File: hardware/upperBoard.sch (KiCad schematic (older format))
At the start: 16 parts, among them J1 Program interface, J2 Conn_02x09_Odd_Even, Q1 S8050, Q2 S8050, SW1 Reset, SW2 Prog, U1 ESP-12F, U2 PCF8575

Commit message: started to replace PCF8575 with MCP23016 and separated LEDs with arrays
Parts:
- removed U2: PCF8575, Package_SO:SSOP-24_5.3x8.2mm_P0.65mm, symbol NXP:PCF8575
- added BAR?: HDSP-4830_2, Display:HDSP-4830, symbol LED:HDSP-4830_2
- added C?: C, symbol Device:C
- added IC?: MCP23016SO, microchip-dspic-SO-28W, symbol microchip-dspic:MCP23016SO
- added R?: R, symbol Device:R
- added RN?: R_Network08, Resistor_THT:R_Array_SIP9, symbol Device:R_Network08
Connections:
- wire segments 148 -> 101

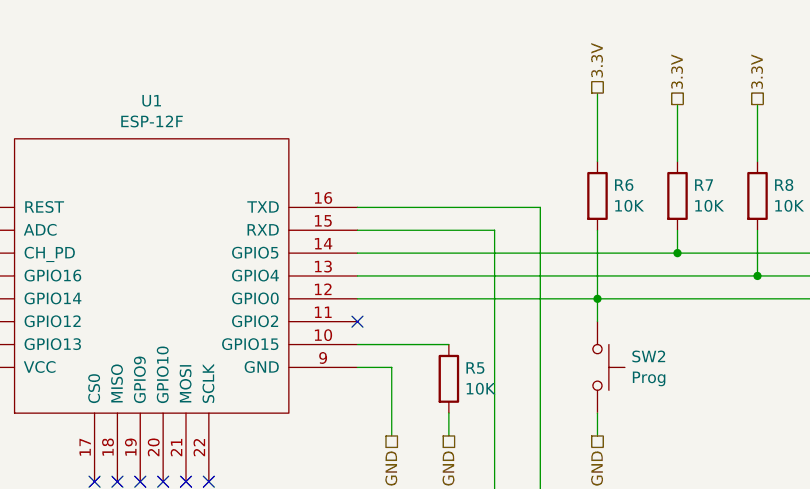
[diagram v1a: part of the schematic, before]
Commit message: renamed hardware files
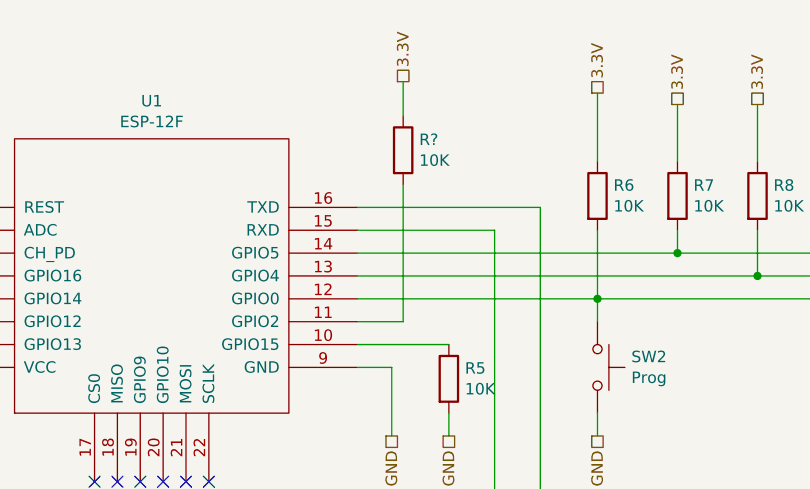
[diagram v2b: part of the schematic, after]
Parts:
- added R?: 10K, Resistor_SMD:R_0201_0603Metric, symbol Device:R
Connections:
- wire segments 101 -> 104
- no-connect marks 13 -> 12
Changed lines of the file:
@@
 NoConn ~ 2600 3000
 NoConn ~ 2500 3000
-NoConn ~ 3650 2300
 NoConn ~ 1850 1900
 NoConn ~ 1850 2100
@@
 	-1   0    0    1
 $EndComp
+$Comp
+L Device:R R?
+U 1 1 5D9733D1
+P 3850 1550
+F 0 "R?" H 3920 1596 50  0000 L CNN
+F 1 "10K" H 3920 1505 50  0000 L CNN
+F 2 "Resistor_SMD:R_0201_0603Metric" V 3780 1550 50  0001 C CNN
+F 3 "~" H 3850 1550 50  0001 C CNN
+	1    3850 1550
+	1    0    0    -1
+$EndComp
+Text HLabel 3850 1250 1    50   UnSpc ~ 0
+3.3V
+Wire Wire Line
+	3850 1250 3850 1400
+Wire Wire Line
+	3850 1700 3850 2300
+Wire Wire Line
+	3850 2300 3650 2300
 $EndSCHEMATC

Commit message: replaced separated driver parts with driver chips and LED bars
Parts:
- removed J2: Conn_02x09_Odd_Even, symbol Connector_Generic:Conn_02x09_Odd_Even
- added BAR1: HDSP-4830_2, Display:HDSP-4830, symbol LED:HDSP-4830_2
- added J2: Conn_02x10_Odd_Even, symbol Connector_Generic:Conn_02x10_Odd_Even
- added RN1: R_Network08, Resistor_THT:R_Array_SIP9, symbol Device:R_Network08
- added U2, U4: A2982, Package_SO:SOIC-20W_7.5x12.8mm_P1.27mm, symbol Transistor_Array:A2982
- gave numbers to parts that had none: 6
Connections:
- net labels added: 1.0, 1.1, 1.2, 1.3, 1.4, 1.5, 1.6, 1.7, 12V
- net labels removed: upper3.3V, upperGND
- wire segments 104 -> 183
- no-connect marks 12 -> 20
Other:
- moved on the sheet: BAR2, C2, J1, Q1, Q2, R1, R10, R2, R3, R4, R5, R6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

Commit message: extracted relay to sub schematic to be able to multiply it
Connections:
- wire segments 183 -> 185
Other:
- moved on the sheet: J2
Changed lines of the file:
@@
 $Descr A4 11693 8268
 encoding utf-8
-Sheet 2 3
+Sheet 2 5
 Title ""
 Date ""
@@
 Wire Wire Line
 	3300 2600 4450 2600
-Text HLabel 5650 7550 0    50   UnSpc ~ 0
-3.3V
-Text HLabel 6550 7550 2    50   UnSpc ~ 0
+Text HLabel 850  5500 0    50   UnSpc ~ 0
+3.3V
+Text HLabel 1750 5500 2    50   UnSpc ~ 0
 GND
 Text HLabel 6700 3350 3    50   UnSpc ~ 0
@@
 Text HLabel 5300 3400 3    50   UnSpc ~ 0
 3.3V
-Text HLabel 5650 7450 0    50   UnSpc ~ 0
+Text HLabel 850  5400 0    50   UnSpc ~ 0
 15
-Text HLabel 5650 7350 0    50   UnSpc ~ 0
+Text HLabel 850  5300 0    50   UnSpc ~ 0
 13
-Text HLabel 5650 7250 0    50   UnSpc ~ 0
+Text HLabel 850  5200 0    50   UnSpc ~ 0
 11
-Text HLabel 5650 7150 0    50   UnSpc ~ 0
+Text HLabel 850  5100 0    50   UnSpc ~ 0
 09
-Text HLabel 5650 7050 0    50   UnSpc ~ 0
+Text HLabel 850  5000 0    50   UnSpc ~ 0
 07
-Text HLabel 5650 6950 0    50   UnSpc ~ 0
+Text HLabel 850  4900 0    50   UnSpc ~ 0
 05
-Text HLabel 5650 6850 0    50   UnSpc ~ 0
+Text HLabel 850  4800 0    50   UnSpc ~ 0
 03
-Text HLabel 5650 6750 0    50   UnSpc ~ 0
+Text HLabel 850  4700 0    50   UnSpc ~ 0
 01
-Text HLabel 6550 7450 2    50   UnSpc ~ 0
+Text HLabel 1750 5400 2    50   UnSpc ~ 0
 16
-Text HLabel 6550 7350 2    50   UnSpc ~ 0
+Text HLabel 1750 5300 2    50   UnSpc ~ 0
 14
-Text HLabel 6550 7250 2    50   UnSpc ~ 0
+Text HLabel 1750 5200 2    50   UnSpc ~ 0
 12
-Text HLabel 6550 7150 2    50   UnSpc ~ 0
+Text HLabel 1750 5100 2    50   UnSpc ~ 0
 10
-Text HLabel 6550 7050 2    50   UnSpc ~ 0
+Text HLabel 1750 5000 2    50   UnSpc ~ 0
 08
-Text HLabel 6550 6950 2    50   UnSpc ~ 0
+Text HLabel 1750 4900 2    50   UnSpc ~ 0
 06
-Text HLabel 6550 6850 2    50   UnSpc ~ 0
+Text HLabel 1750 4800 2    50   UnSpc ~ 0
 04
-Text HLabel 6550 6750 2    50   UnSpc ~ 0
+Text HLabel 1750 4700 2    50   UnSpc ~ 0
 02
 Wire Wire Line
-	5650 6750 5850 6750
-Wire Wire Line
-	5850 6850 5650 6850
-Wire Wire Line
-	5650 6950 5850 6950
-Wire Wire Line
-	5850 7050 5650 7050
-Wire Wire Line
-	5650 7150 5850 7150
-Wire Wire Line
-	5850 7250 5650 7250
-Wire Wire Line
-	5850 7550 5650 7550
-Wire Wire Line
-	6350 6750 6550 6750
-Wire Wire Line
-	6350 6850 6550 6850
-Wire Wire Line
-	6550 6950 6350 6950
-Wire Wire Line
-	6550 7050 6350 7050
-Wire Wire Line
-	6550 7150 6350 7150
-Wire Wire Line
-	6550 7250 6350 7250
-Wire Wire Line
-	6550 7350 6350 7350
-Wire Wire Line
-	6550 7450 6350 7450
+	850  4700 1050 4700
+Wire Wire Line
+	1050 4800 850  4800
+Wire Wire Line
+	850  4900 1050 4900
+Wire Wire Line
+	1050 5000 850  5000
+Wire Wire Line
+	850  5100 1050 5100
+Wire Wire Line
+	1050 5200 850  5200
+Wire Wire Line
+	1050 5500 850  5500
+Wire Wire Line
+	1550 4700 1750 4700
+Wire Wire Line
+	1550 4800 1750 4800
+Wire Wire Line
+	1750 4900 1550 4900
+Wire Wire Line
+	1750 5000 1550 5000
+Wire Wire Line
+	1750 5100 1550 5100
+Wire Wire Line
+	1750 5200 1550 5200
+Wire Wire Line
+	1750 5300 1550 5300
+Wire Wire Line
+	1750 5400 1550 5400
 Text HLabel 8450 4950 2    50   UnSpc ~ 0
 16
 Wire Wire Line
-	5850 7350 5650 7350
-Wire Wire Line
-	5850 7450 5650 7450
-Wire Wire Line
-	6350 7550 6550 7550
+	1050 5300 850  5300
+Wire Wire Line
+	1050 5400 850  5400
+Wire Wire Line
+	1550 5500 1750 5500
 $Comp
 L microchip-dspic:MCP23016SO IC1
@@
 L Connector_Generic:Conn_02x10_Odd_Even J2
 U 1 1 5DAC3666
-P 6050 7150
-F 0 "J2" H 6100 7767 50  0000 C CNN
-F 1 "Conn_02x10_Odd_Even" H 6100 7676 50  0000 C CNN
-F 2 "" H 6050 7150 50  0001 C CNN
-F 3 "~" H 6050 7150 50  0001 C CNN
-	1    6050 7150
-	1    0    0    -1
-$EndComp
-Text HLabel 6550 7650 2    50   UnSpc ~ 0
-GND
-Wire Wire Line
-	6550 7650 6350 7650
-Text HLabel 5650 7650 0    50   UnSpc ~ 0
+P 1250 5100
+F 0 "J2" H 1300 5717 50  0000 C CNN
+F 1 "Conn_02x10_Odd_Even" H 1300 5626 50  0000 C CNN
+F 2 "" H 1250 5100 50  0001 C CNN
+F 3 "~" H 1250 5100 50  0001 C CNN
+	1    1250 5100
+	1    0    0    -1
+$EndComp
+Text HLabel 1750 5600 2    50   UnSpc ~ 0
+GND
+Wire Wire Line
+	1750 5600 1550 5600
+Text HLabel 850  5600 0    50   UnSpc ~ 0
 12V
 Wire Wire Line
-	5850 7650 5650 7650
+	1050 5600 850  5600
 Text HLabel 7750 3900 0    50   UnSpc ~ 0
 12V
@@
 NoConn ~ 7150 2450
 NoConn ~ 7150 2850
+Text HLabel 9050 1600 2    50   UnSpc ~ 0
+01
+Text HLabel 9050 1700 2    50   UnSpc ~ 0
+02
+Wire Wire Line
+	8950 1600 9050 1600
+Wire Wire Line
+	8950 1700 9050 1700
 Wire Bus Line
 	6050 3750 6050 4850

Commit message: finished schematic mostly
started to create lower PCB
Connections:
- wire segments 185 -> 198
- no-connect marks 20 -> 21
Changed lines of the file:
@@
 $Descr A4 11693 8268
 encoding utf-8
-Sheet 2 5
+Sheet 2 19
 Title ""
 Date ""
@@
 Wire Wire Line
 	8950 1700 9050 1700
+Text HLabel 9050 1800 2    50   UnSpc ~ 0
+03
+Text HLabel 9050 1900 2    50   UnSpc ~ 0
+04
+Text HLabel 9050 2000 2    50   UnSpc ~ 0
+05
+Text HLabel 9050 2100 2    50   UnSpc ~ 0
+06
+Text HLabel 9050 2200 2    50   UnSpc ~ 0
+07
+Text HLabel 9050 2300 2    50   UnSpc ~ 0
+08
+Wire Wire Line
+	8950 1800 9050 1800
+Wire Wire Line
+	8950 1900 9050 1900
+Wire Wire Line
+	8950 2000 9050 2000
+Wire Wire Line
+	8950 2100 9050 2100
+Wire Wire Line
+	8950 2200 9050 2200
+Wire Wire Line
+	8950 2300 9050 2300
+Text HLabel 8450 4250 2    50   UnSpc ~ 0
+09
+Text HLabel 8450 4850 2    50   UnSpc ~ 0
+15
+Text HLabel 8450 4750 2    50   UnSpc ~ 0
+14
+Text HLabel 8450 4650 2    50   UnSpc ~ 0
+13
+Text HLabel 8450 4550 2    50   UnSpc ~ 0
+12
+Text HLabel 8450 4450 2    50   UnSpc ~ 0
+11
+Text HLabel 8450 4350 2    50   UnSpc ~ 0
+10
+Wire Wire Line
+	8300 4250 8450 4250
+Wire Wire Line
+	8300 4350 8450 4350
+Wire Wire Line
+	8300 4450 8450 4450
+Wire Wire Line
+	8300 4550 8450 4550
+Wire Wire Line
+	8300 4650 8450 4650
+Wire Wire Line
+	8300 4750 8450 4750
+Wire Wire Line
+	8300 4850 8450 4850
+NoConn ~ 6400 2800
 Wire Bus Line
 	6050 3750 6050 4850

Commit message: started to replace MCP23016 with MCP23017
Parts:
- removed Q1, Q2: S8050, Package_TO_SOT_THT:TO-92_Inline, symbol Transistor_BJT:S8050
- added Q? (x2): MMBT3904, Package_TO_SOT_SMD:SOT-23, symbol Transistor_BJT:MMBT3904
- added U?: MCP23017_SO, Package_SO:SOIC-28W_7.5x17.9mm_P1.27mm, symbol Interface_Expansion:MCP23017_SO
- R3, R4: value 12K -> 10K
- R5: value 10K -> 4.7K
- RN2: value R_Network08 -> 150
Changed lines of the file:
@@
 EESchema Schematic File Version 4
-LIBS:relays-device-cache
 EELAYER 30 0
 EELAYER END
 $Descr A4 11693 8268
 encoding utf-8
-Sheet 2 19
+Sheet 1 1
 Title ""
 Date ""
@@
 P 3450 3050
 F 0 "R5" H 3520 3096 50  0000 L CNN
-F 1 "10K" H 3520 3005 50  0000 L CNN
+F 1 "4.7K" H 3520 3005 50  0000 L CNN
 F 2 "Resistor_SMD:R_0201_0603Metric" V 3380 3050 50  0001 C CNN
 F 3 "~" H 3450 3050 50  0001 C CNN
@@
 	4100 4650 4100 4850
 $Comp
-L Transistor_BJT:S8050 Q1
-U 1 1 5D9C1859
-P 2400 4250
-F 0 "Q1" H 2591 4296 50  0000 L CNN
-F 1 "S8050" H 2591 4205 50  0000 L CNN
-F 2 "Package_TO_SOT_THT:TO-92_Inline" H 2600 4175 50  0001 L CIN
-F 3 "http://www.unisonic.com.tw/datasheet/S8050.pdf" H 2400 4250 50  0001 L CNN
-	1    2400 4250
-	-1   0    0    -1
-$EndComp
-$Comp
-L Transistor_BJT:S8050 Q2
-U 1 1 5D9C185F
-P 2400 4900
-F 0 "Q2" H 2591 4854 50  0000 L CNN
-F 1 "S8050" H 2591 4945 50  0000 L CNN
-F 2 "Package_TO_SOT_THT:TO-92_Inline" H 2600 4825 50  0001 L CIN
-F 3 "http://www.unisonic.com.tw/datasheet/S8050.pdf" H 2400 4900 50  0001 L CNN
-	1    2400 4900
-	-1   0    0    1
-$EndComp
-$Comp
 L Device:R R3
 U 1 1 5D9C1865
 P 2850 4250
 F 0 "R3" V 2643 4250 50  0000 C CNN
-F 1 "12K" V 2734 4250 50  0000 C CNN
+F 1 "10K" V 2734 4250 50  0000 C CNN
 F 2 "Resistor_SMD:R_0201_0603Metric" V 2780 4250 50  0001 C CNN
 F 3 "~" H 2850 4250 50  0001 C CNN
@@
 P 2850 4900
 F 0 "R4" V 2643 4900 50  0000 C CNN
-F 1 "12K" V 2734 4900 50  0000 C CNN
+F 1 "10K" V 2734 4900 50  0000 C CNN
 F 2 "Resistor_SMD:R_0201_0603Metric" V 2780 4900 50  0001 C CNN
 F 3 "~" H 2850 4900 50  0001 C CNN
@@
 P 7650 3150
 F 0 "RN2" H 7170 3104 50  0000 R CNN
-F 1 "R_Network08" H 7170 3195 50  0000 R CNN
+F 1 "150" H 7170 3195 50  0000 R CNN
 F 2 "Resistor_THT:R_Array_SIP9" V 8125 3150 50  0001 C CNN
 F 3 "http://www.vishay.com/docs/31509/csc.pdf" H 7650 3150 50  0001 C CNN
@@
 	8300 4850 8450 4850
 NoConn ~ 6400 2800
+$Comp
+L Transistor_BJT:MMBT3904 Q?
+U 1 1 5FE4541A
+P 2400 4900
+F 0 "Q?" H 2591 4854 50  0000 L CNN
+F 1 "MMBT3904" H 2591 4945 50  0000 L CNN
+F 2 "Package_TO_SOT_SMD:SOT-23" H 2600 4825 50  0001 L CIN
+F 3 "https://www.onsemi.com/pub/Collateral/2N3903-D.PDF" H 2400 4900 50  0001 L CNN
+	1    2400 4900
+	-1   0    0    1
+$EndComp
+$Comp
+L Transistor_BJT:MMBT3904 Q?
+U 1 1 5FE53400
+P 2400 4250
+F 0 "Q?" H 2591 4296 50  0000 L CNN
+F 1 "MMBT3904" H 2591 4205 50  0000 L CNN
+F 2 "Package_TO_SOT_SMD:SOT-23" H 2600 4175 50  0001 L CIN
+F 3 "https://www.onsemi.com/pub/Collateral/2N3903-D.PDF" H 2400 4250 50  0001 L CNN
+	1    2400 4250
+	-1   0    0    -1
+$EndComp
 Wire Bus Line
 	6050 3750 6050 4850
 Wire Bus Line
 	5200 900  5200 2200
+$Comp
+L Interface_Expansion:MCP23017_SO U?
+U 1 1 5FF85679
+P 10550 2250
+F 0 "U?" H 10550 3531 50  0000 C CNN
+F 1 "MCP23017_SO" H 10550 3440 50  0000 C CNN
+F 2 "Package_SO:SOIC-28W_7.5x17.9mm_P1.27mm" H 10750 1250 50  0001 L CNN
+F 3 "http://ww1.microchip.com/downloads/en/DeviceDoc/20001952C.pdf" H 10750 1150 50  0001 L CNN
+	1    10550 2250
+	1    0    0    -1
+$EndComp
 $EndSCHEMATC

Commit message: replaced MCP23016 with MCP23017
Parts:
- removed C2: C, symbol Device:C
- removed IC1: MCP23016SO, microchip-dspic-SO-28W, symbol microchip-dspic:MCP23016SO
- removed R10: R, symbol Device:R
- gave numbers to parts that had none: 3
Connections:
- net labels removed: 1.0, 1.1, 1.2, 1.3, 1.4, 1.5, 1.6, 1.7
- wire segments 198 -> 197
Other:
- moved on the sheet: BAR1, BAR2, RN1, RN2, U2, U3, U4
